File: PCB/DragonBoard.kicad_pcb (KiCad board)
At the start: 2 copper layers, 143.4 x 111.8 mm, 120 parts, among them J3 OLED, Q1 2N7002, Q2 AO3401A, SW1 SW_PUSH_LED, SW10 SW_PUSH_LED, SW11 SW_PUSH_LED, SW12 SW_PUSH_LED, SW13 SW_PUSH_LED, SW14 SW_PUSH_LED, SW15 SW_PUSH_LED, SW16 SW_PUSH_LED, SW17 SW_PUSH_LED, SW18 SW_PUSH_LED, SW19 SW_PUSH_LED, SW2 SW_PUSH_LED, SW20 SW_PUSH_LED, SW21 SW_PUSH_LED, SW22 SW_PUSH_LED, SW23 SW_PUSH_LED, SW24 SW_PUSH_LED, SW26 SW_PUSH_LED, SW27 SW_PUSH_LED, SW28 SW_PUSH_LED, SW29 SW_PUSH_LED, SW3 SW_PUSH_LED, SW30 SW_PUSH_LED, SW31 Rotary_Encoder_Switch, SW4 SW_PUSH_LED, SW5 SW_PUSH_LED, SW6 SW_PUSH_LED, SW7 SW_PUSH_LED, SW8 SW_PUSH_LED, SW9 SW_PUSH_LED, U1 ProMicro

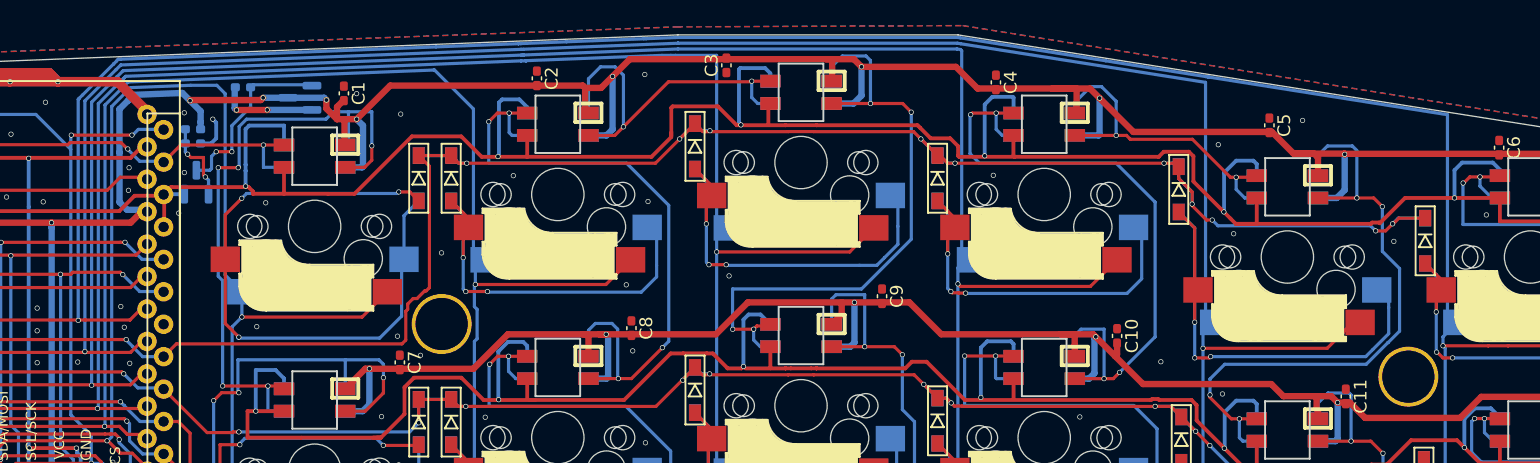
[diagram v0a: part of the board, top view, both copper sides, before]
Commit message: fix remaining DFM checks
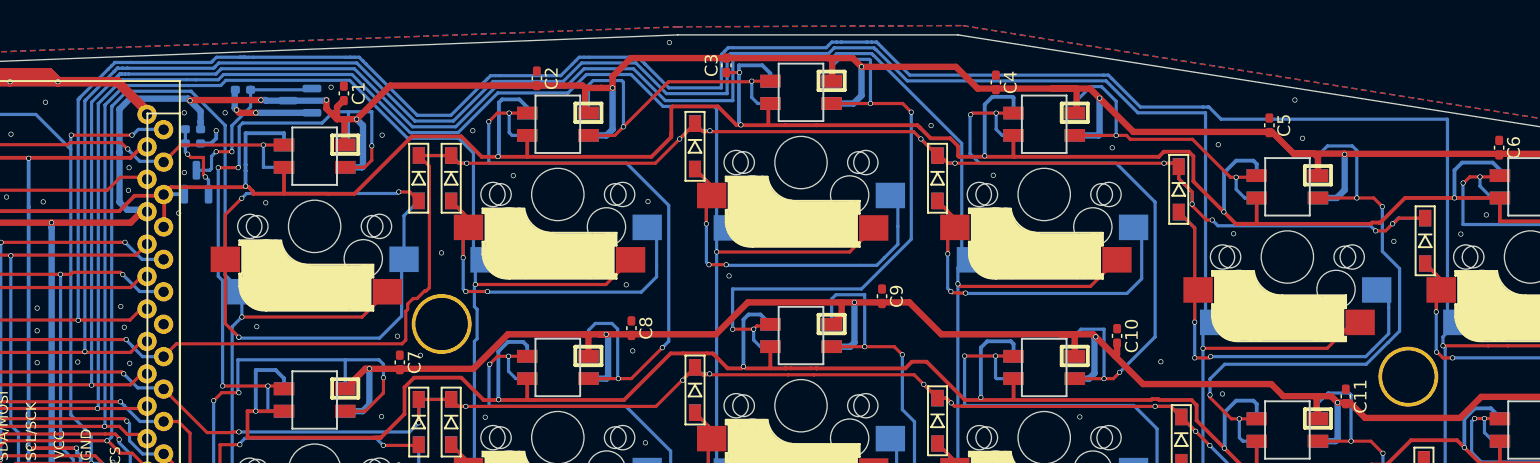
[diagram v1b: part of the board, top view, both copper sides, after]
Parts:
- moved Q2 0.23 mm to (119.4, 40.2)
- moved R3 0.20 mm to (114.9, 39.3)
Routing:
- net col0: track 342.8 -> 352.8 mm
- net col1: track 326.2 -> 333.7 mm
- net col2: track 305.9 -> 309.7 mm
- net col4: track 270.3 -> 267.8 mm
- net col5: track 200.9 -> 199.1 mm
- net Net-(SW2B-DOUT): track 29.1 -> 27.6 mm
- net VCC: track 929.6 -> 928.9 mm
- net col3: track 294.8 -> 295.5 mm
- net GND: track 1126.3 -> 1125.6 mm, vias 156 -> 163
